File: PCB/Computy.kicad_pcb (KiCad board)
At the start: 2 copper layers, 50 x 100 mm, 44 parts, among them J1 USB_C_Receptacle_USB2.0_16P, J2 Conn_ARM_JTAG_SWD_10, J3 Conn_01x03_Socket, J4 Conn_01x04_Socket, J5 Conn_02x04_Odd_Even, M1 Motor_Servo, M2 Motor_Servo, M3 Motor_Servo, M4 Motor_Servo, M5 Motor_Servo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

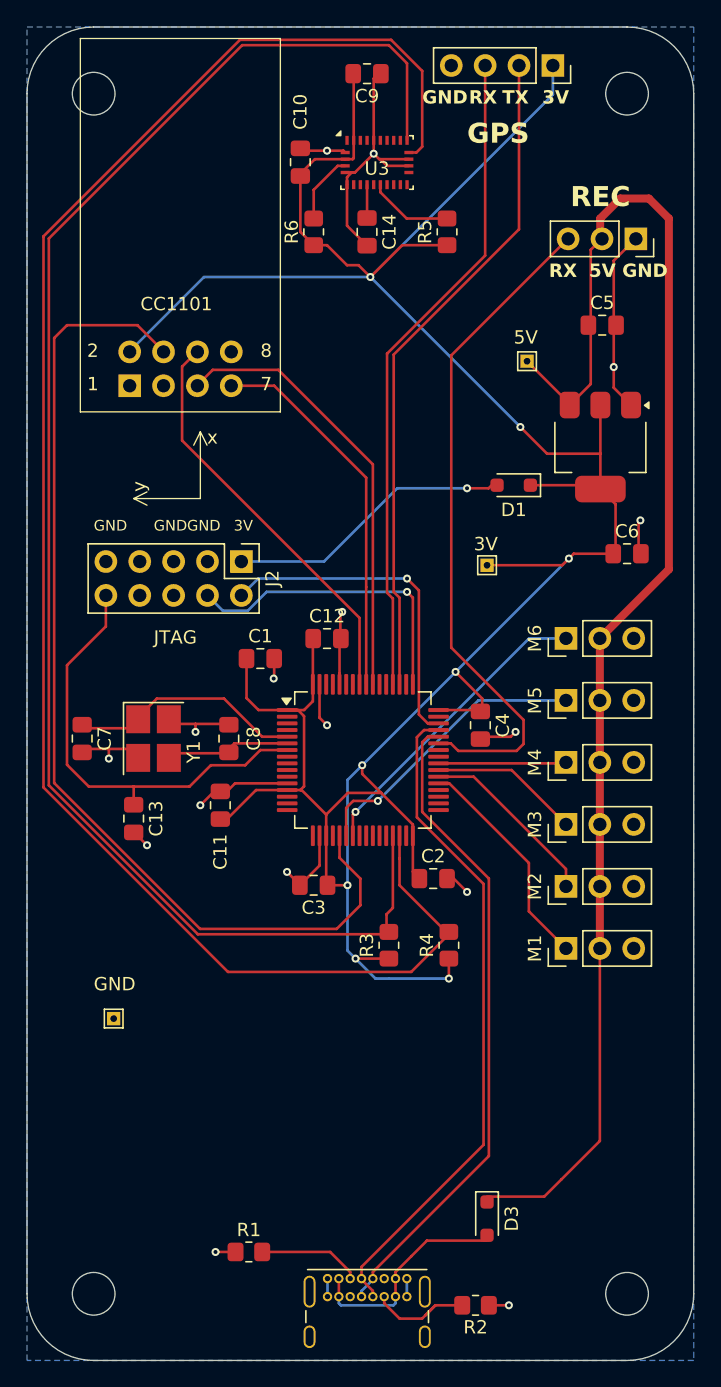
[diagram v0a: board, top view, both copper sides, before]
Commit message: Computy v2
- Fix issues with the PCB
    - Connect SWO
    - Connect CC1101 to SPI1
    - Fix BNO055 SCL and SDA
    - Add more testpoints
- Update firmware
- Add most recent datasheets
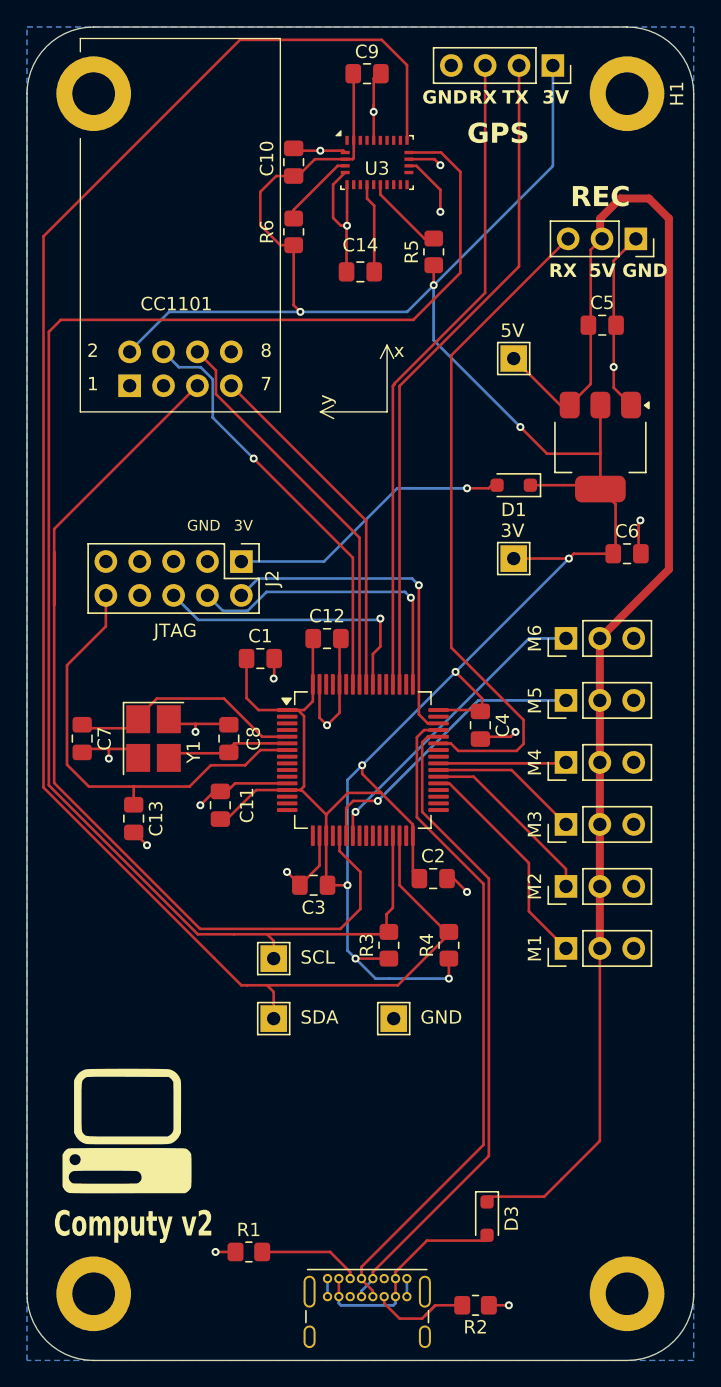
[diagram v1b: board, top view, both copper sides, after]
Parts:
- added G***: LOGO, LOGO, F.Cu at (92.5, 123.0)
- added TP4: TP_SDA, TestPoint:TestPoint_THTPad_2.0x2.0mm_Drill1.0mm, F.Cu at (103.5, 114.5)
- added TP5: TP_SCL, TestPoint:TestPoint_THTPad_2.0x2.0mm_Drill1.0mm, F.Cu at (103.5, 110.0)
- H1, H2, H3, H4: footprint MountingHole:MountingHole_3.2mm_M3 -> MountingHole:MountingHole_3.2mm_M3_DIN965_Pad
- R3, R4: value 10k -> 4.7k
- TP1: value TestPoint_Probe -> TP_5V; footprint TestPoint:TestPoint_THTPad_1.0x1.0mm_Drill0.5mm -> TestPoint:TestPoint_THTPad_2.0x2.0mm_Drill1.0mm
- TP2: value TestPoint_Probe -> TP_3.3V; footprint TestPoint:TestPoint_THTPad_1.0x1.0mm_Drill0.5mm -> TestPoint:TestPoint_THTPad_2.0x2.0mm_Drill1.0mm
- TP3: value TestPoint_Probe -> TestPoint_GND; footprint TestPoint:TestPoint_THTPad_1.0x1.0mm_Drill0.5mm -> TestPoint:TestPoint_THTPad_2.0x2.0mm_Drill1.0mm
- moved TP3 21.0 mm to (112.5, 114.5)
- moved C14 3.04 mm to (110.0, 58.5), turned to 180 degrees
- moved TP2 2.06 mm to (121.5, 80.0)
- moved R5 1.80 mm to (115.5, 57.0)
- moved R6 1.50 mm to (105.0, 55.5)
- moved TP1 1.02 mm to (121.5, 65.0)
- moved C10 0.50 mm to (105.0, 50.3)
- turned H4 to 0 degrees
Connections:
- net /SPI3_MISO renamed /SPI1_MISO
- net /SPI3_MOSI renamed /SPI1_MOSI
- J2 pad 6: unconnected-(J2-SWO/TDO-Pad6) -> /SWO
- J5 pad 5: /SPI3_SCK -> /SPI1_SCK
- U1 pad 21: /CC1101_CSN -> /SPI1_SCK
- U1 pad 55: /SPI3_SCK -> /SWO
- U1 pad 58: unconnected-(U1-PB6-Pad58) -> /CC1101_CSN
- U3 pad 19: /I2C2_SDA -> /I2C2_SCL
- U3 pad 20: /I2C2_SCL -> /I2C2_SDA
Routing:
- net /SPI1_SCK: track 0.00 -> 72.5 mm
- net /CC1101_CSN: track 76.9 -> 31.8 mm, vias 0 -> 1
- net /SPI3_SCK: track 33.1 -> 0.00 mm
- net /SWO: track 0.00 -> 21.5 mm, vias 0 -> 1
- net GND: track 86.6 -> 92.0 mm, vias 16 -> 18
- net Net-(U3-CAP): track 2.50 -> 6.76 mm
- net +3.3V: track 227.5 -> 223.5 mm, vias 8 -> 9
- net /SPI1_MISO: track 28.5 -> 26.6 mm
- net +5V: track 107.5 -> 108.6 mm
- net /I2C2_SDA: track 129.9 -> 130.9 mm
- net /SPI1_MOSI: track 31.0 -> 30.0 mm
- net Net-(U3-~{BOOT_LOAD_PIN}): track 5.26 -> 5.88 mm
- net /I2C2_SCL: track 118.1 -> 118.6 mm
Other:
- board text added: "Computy v2"
- board text added: "SCL"
- board text added: "SDA"
